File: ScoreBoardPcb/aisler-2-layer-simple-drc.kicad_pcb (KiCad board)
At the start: 2 copper layers, 95 x 75 mm, 16 parts, among them J1 Conn_02x20_Odd_Even, U1 CD4066BM96, U2 CD4066BM96, U3 CD4066BM96, U4 CD4066BM96, U5 ADM3101EARQZ-REEL

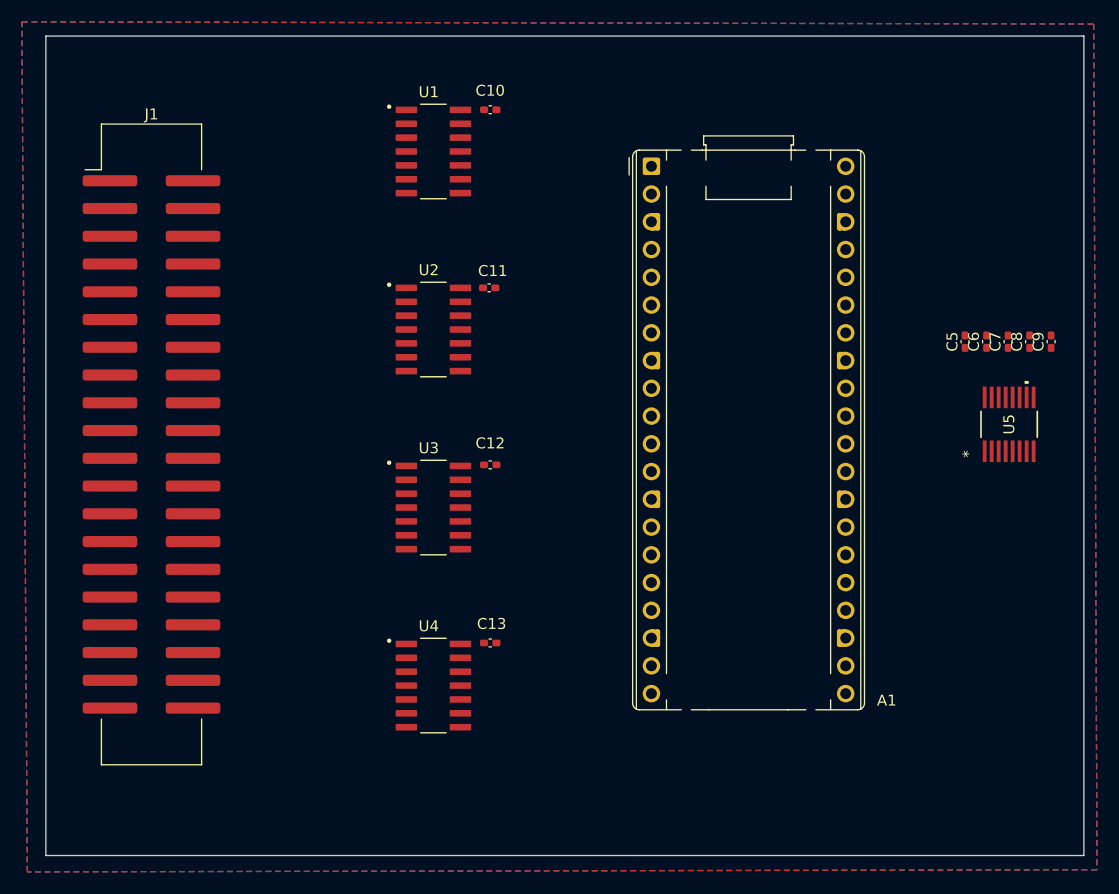
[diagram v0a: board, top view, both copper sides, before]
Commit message: Routed with mounting holes
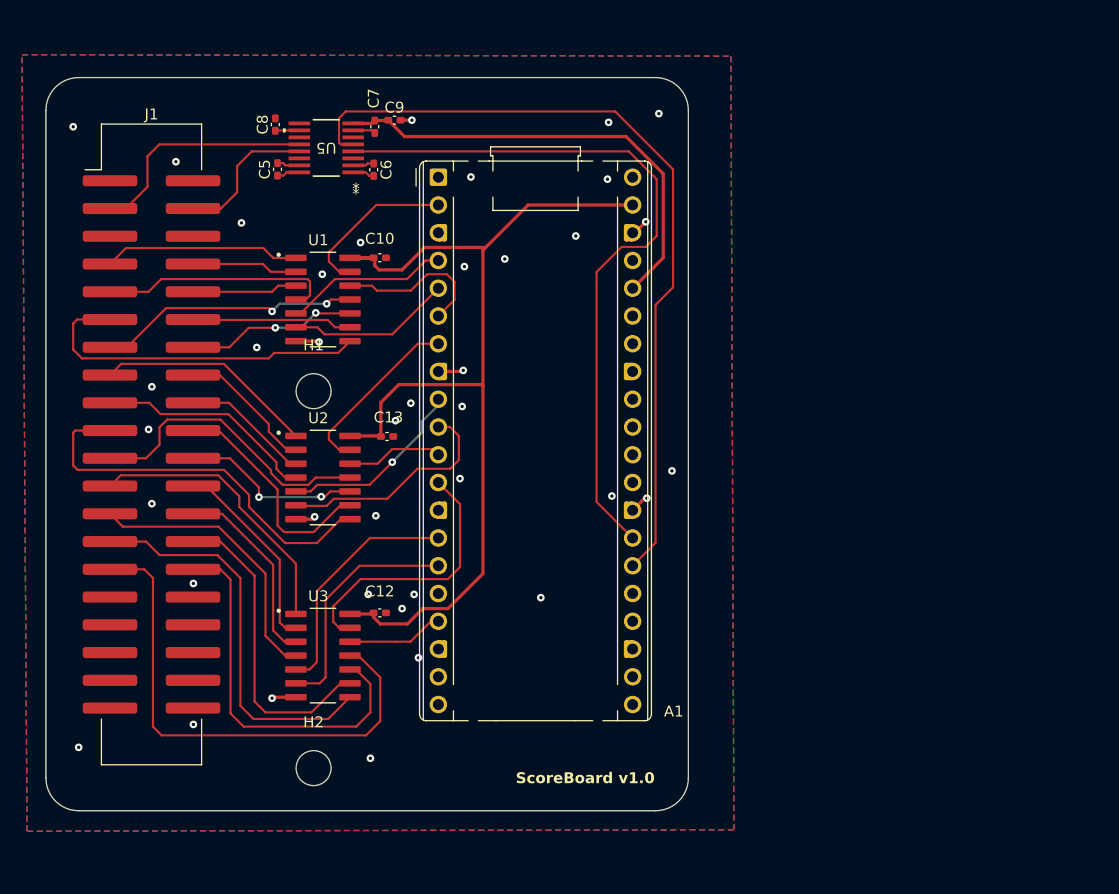
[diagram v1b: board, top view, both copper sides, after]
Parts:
- removed C11: 0.1uF, Capacitor_SMD:C_0402_1005Metric_Pad0.74x0.62mm_HandSolder
- removed U4: CD4066BM96, ScoreBoardPcb:SOIC127P600X175-14N
- added H1: MountingHole, MountingHole:MountingHole_3.2mm_M3, F.Cu at (124.5, 82.5)
- added H2: MountingHole, MountingHole:MountingHole_3.2mm_M3, F.Cu at (124.5, 117.0)
- moved C8 71.8 mm to (121.0, 58.1)
- moved U5 67.4 mm to (125.7, 60.2), turned to 180 degrees
- moved C5 64.9 mm to (121.2, 62.2)
- moved C9 63.4 mm to (131.9, 57.7), turned to 0 degrees
- moved C7 61.2 mm to (130.1, 58.3), turned to -90 degrees
- moved C6 58.3 mm to (130.0, 62.2), turned to -90 degrees
- moved C13 21.1 mm to (131.2, 86.6)
- moved A1 19.5 mm to (135.9, 62.9)
- moved C10 16.9 mm to (130.6, 70.3)
- moved U1 16.9 mm to (125.4, 74.1)
- moved U2 16.9 mm to (125.4, 90.4)
- moved U3 16.9 mm to (125.4, 106.7)
- moved C12 16.9 mm to (130.6, 102.8)
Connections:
- A1 pad 10: unconnected-(A1-GPIO7-Pad10) -> /MIN_INC
- A1 pad 11: unconnected-(A1-GPIO8-Pad11) -> /MIN_DEC
- A1 pad 12: unconnected-(A1-GPIO9-Pad12) -> /SEC_INC
- A1 pad 14: unconnected-(A1-GPIO10-Pad14) -> /SEC_DEC
- A1 pad 15: unconnected-(A1-GPIO11-Pad15) -> /CLEAR
- A1 pad 17: unconnected-(A1-GPIO13-Pad17) -> /AUX
- A1 pad 21: /TX_TTL -> unconnected-(A1-GPIO16-Pad21)
- A1 pad 22: /RX_TTL -> unconnected-(A1-GPIO17-Pad22)
- A1 pad 26: unconnected-(A1-GPIO20-Pad26) -> /TX_TTL
- A1 pad 27: unconnected-(A1-GPIO21-Pad27) -> /RX_TTL
- J1 pad 19: unconnected-(J1-Pin_19-Pad19) -> /MIN_INC_1
- J1 pad 20: unconnected-(J1-Pin_20-Pad20) -> /MIN_INC_2
- J1 pad 21: unconnected-(J1-Pin_21-Pad21) -> /MIN_DEC_1
- J1 pad 22: unconnected-(J1-Pin_22-Pad22) -> /MIN_DEC_2
- J1 pad 23: unconnected-(J1-Pin_23-Pad23) -> /SEC_INC_1
- J1 pad 24: unconnected-(J1-Pin_24-Pad24) -> /SEC_INC_2
- J1 pad 25: unconnected-(J1-Pin_25-Pad25) -> /SEC_DEC_1
- J1 pad 26: unconnected-(J1-Pin_26-Pad26) -> /SEC_DEC_2
- J1 pad 27: unconnected-(J1-Pin_27-Pad27) -> /CLEAR_1
- J1 pad 28: unconnected-(J1-Pin_28-Pad28) -> /CLEAR_2
- J1 pad 29: unconnected-(J1-Pin_29-Pad29) -> /AUX_1
- J1 pad 30: unconnected-(J1-Pin_30-Pad30) -> /AUX_2
- J1 pad 31: unconnected-(J1-Pin_31-Pad31) -> GND
- J1 pad 32: unconnected-(J1-Pin_32-Pad32) -> GND
- J1 pad 33: unconnected-(J1-Pin_33-Pad33) -> GND
- J1 pad 34: unconnected-(J1-Pin_34-Pad34) -> GND
- J1 pad 35: unconnected-(J1-Pin_35-Pad35) -> GND
- J1 pad 36: unconnected-(J1-Pin_36-Pad36) -> GND
- J1 pad 37: unconnected-(J1-Pin_37-Pad37) -> GND
- J1 pad 38: unconnected-(J1-Pin_38-Pad38) -> GND
- J1 pad 39: unconnected-(J1-Pin_39-Pad39) -> GND
- J1 pad 40: unconnected-(J1-Pin_40-Pad40) -> GND
- J1 pad 5: unconnected-(J1-Pin_5-Pad5) -> GND
- J1 pad 6: unconnected-(J1-Pin_6-Pad6) -> GND
- U2 pad 10: unconnected-(U2-SIG_D_OUT/IN-Pad10) -> /MIN_DEC_2
- U2 pad 11: unconnected-(U2-SIG_D_IN/OUT-Pad11) -> /MIN_DEC_1
- U2 pad 12: unconnected-(U2-CONTROL_D-Pad12) -> /MIN_DEC
- U2 pad 6: unconnected-(U2-CONTROL_C-Pad6) -> /MIN_INC
- U2 pad 8: unconnected-(U2-SIG_C_IN/OUT-Pad8) -> /MIN_INC_1
- U2 pad 9: unconnected-(U2-SIG_C_OUT/IN-Pad9) -> /MIN_INC_2
- U3 pad 1: unconnected-(U3-SIG_A_IN/OUT-Pad1) -> /SEC_INC_1
- U3 pad 10: unconnected-(U3-SIG_D_OUT/IN-Pad10) -> /AUX_2
- U3 pad 11: unconnected-(U3-SIG_D_IN/OUT-Pad11) -> /AUX_1
- U3 pad 12: unconnected-(U3-CONTROL_D-Pad12) -> /AUX
- U3 pad 13: unconnected-(U3-CONTROL_A-Pad13) -> /SEC_INC
- U3 pad 2: unconnected-(U3-SIG_A_OUT/IN-Pad2) -> /SEC_INC_2
- U3 pad 3: unconnected-(U3-SIG_B_OUT/IN-Pad3) -> /SEC_DEC_2
- U3 pad 4: unconnected-(U3-SIG_B_IN/OUT-Pad4) -> /SEC_DEC_1
- U3 pad 5: unconnected-(U3-CONTROL_B-Pad5) -> /SEC_DEC
- U3 pad 6: unconnected-(U3-CONTROL_C-Pad6) -> /CLEAR
- U3 pad 8: unconnected-(U3-SIG_C_IN/OUT-Pad8) -> /CLEAR_1
- U3 pad 9: unconnected-(U3-SIG_C_OUT/IN-Pad9) -> /CLEAR_2
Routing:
- net +5V: track 0.00 -> 91.7 mm
- net /TX_TTL: track 0.00 -> 74.4 mm
- net /RX_TTL: track 0.00 -> 66.6 mm
- net /AUX_1: track 0.00 -> 47.1 mm
- net +3.3V: track 0.00 -> 42.1 mm
- net /CLEAR_1: track 0.00 -> 36.4 mm
- net /MIN_INC_1: track 0.00 -> 35.4 mm
- net /AUX_2: track 0.00 -> 34.9 mm
- net /HOME_DEC_1: track 0.00 -> 32.2 mm
- net /CLEAR_2: track 0.00 -> 27.8 mm
- net /MIN_DEC_1: track 0.00 -> 27.3 mm
- net /SEC_INC_1: track 0.00 -> 26.0 mm
- net /SEC_DEC_1: track 0.00 -> 25.7 mm
- net /SEC_INC: track 0.00 -> 24.8 mm
- net /AWAY_INC_1: track 0.00 -> 22.8 mm, vias 0 -> 2
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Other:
- board size 95 x 75 mm -> 58.8 x 67.1 mm
- board text added: "ScoreBoard v1.0"

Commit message: Update to use CD74HCT4066M96
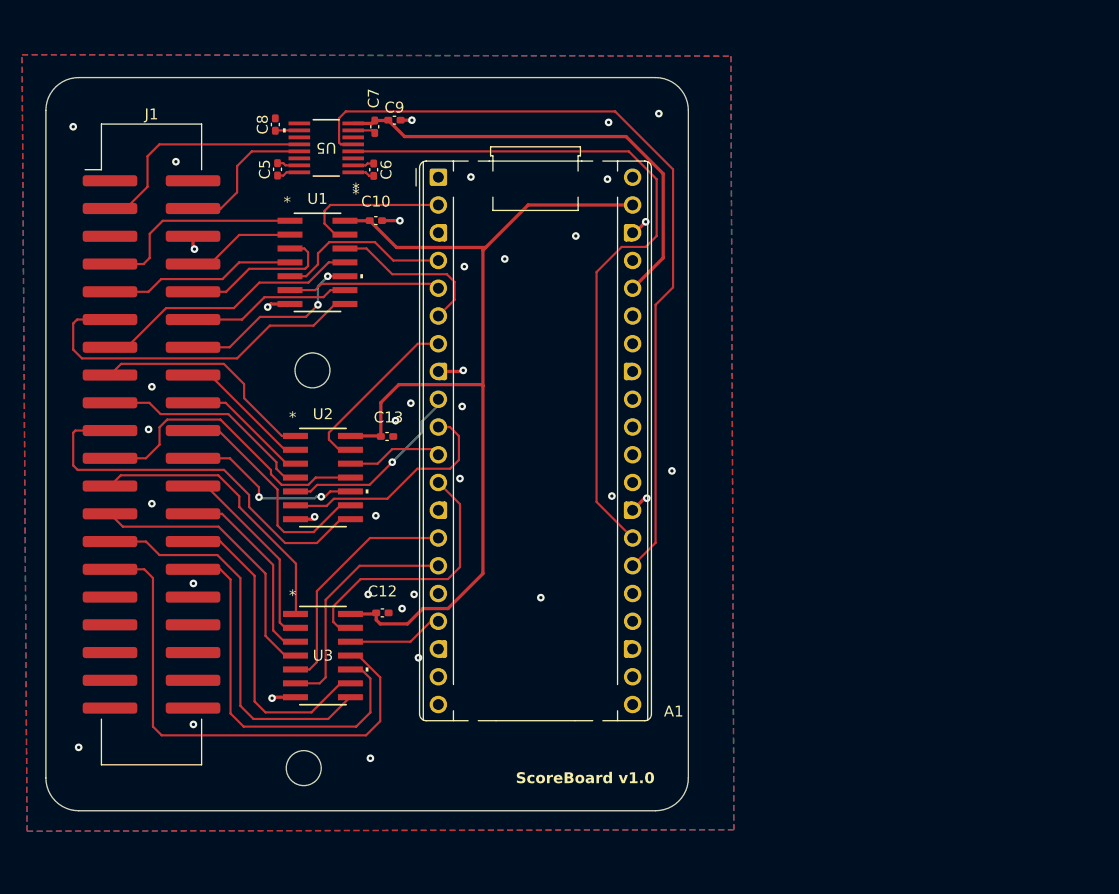
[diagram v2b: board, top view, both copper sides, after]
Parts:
- U1, U2, U3: value CD4066BM96 -> CD74HCT4066M96; footprint ScoreBoardPcb:SOIC127P600X175-14N -> ScoreBoardPcb:D14-M
- moved U1 3.44 mm to (124.9, 70.7)
- moved C10 3.42 mm to (130.2, 66.9)
- moved H1 1.90 mm to (124.4, 80.6)
- moved H2 0.90 mm to (123.6, 117.0)
- moved C12 0.24 mm to (130.8, 102.8)
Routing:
- net /HOME_INC_2: track 9.65 -> 14.6 mm
- net /HOME_INC_1: track 21.6 -> 17.6 mm
- net GND: track 12.9 -> 15.6 mm, vias 39 -> 37
- net /AWAY_DEC_2: track 11.8 -> 9.68 mm
- net +5V: track 91.7 -> 89.6 mm
- net /AWAY_INC_2: track 15.7 -> 17.6 mm
- net /START: track 15.0 -> 13.2 mm
- net /HOME_DEC: track 15.1 -> 13.4 mm
- net /HOME_INC: track 14.6 -> 16.2 mm
- net /START_1: track 18.0 -> 19.4 mm
- net /START_2: track 9.71 -> 8.39 mm
- net /SEC_DEC_2: track 17.4 -> 16.4 mm
- net /AWAY_DEC: track 16.3 -> 15.4 mm
- net /SEC_INC: track 24.8 -> 23.8 mm
- net /SEC_INC_2: track 16.9 -> 16.0 mm
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
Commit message: Rev 1.0 submitted for manf
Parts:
- A1: footprint Module:RaspberryPi_Pico_Common_THT -> ScoreBoardPcb:RaspberryPi_Pico_Common_THT
- moved H1 26.5 mm to (120.5, 54.4)
- moved C8 6.44 mm to (119.9, 64.4), turned to 180 degrees
- moved U5 5.79 mm to (124.9, 66.0)
- moved C5 5.78 mm to (120.6, 67.9)
- moved C6 5.77 mm to (129.5, 68.0)
- moved C7 5.77 mm to (129.6, 64.0)
- moved C9 5.77 mm to (131.4, 63.4)
- moved C10 5.75 mm to (130.4, 72.6)
- moved U1 5.75 mm to (124.9, 76.5)
- moved U3 4.52 mm to (124.8, 102.2)
- moved C12 4.42 mm to (130.3, 98.4)
- moved H2 3.16 mm to (120.5, 116.4)
- moved C13 1.47 mm to (130.3, 85.5)
- moved U2 1.18 mm to (124.9, 89.3)
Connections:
- A1 pad 39: +5V -> unconnected-(A1-VSYS-Pad39)
- J1 pad 2: GND -> +5V
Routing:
- net /AUX_2: track 34.2 -> 12.6 mm, vias 0 -> 2
- net /TX_TTL: track 74.4 -> 61.7 mm
- net /AUX_1: track 46.4 -> 34.0 mm
- net /CLEAR_2: track 27.8 -> 15.6 mm
- net +5V: track 89.6 -> 100.4 mm
- net /CLEAR_1: track 36.4 -> 26.4 mm
- net /RX_TTL: track 66.6 -> 56.9 mm
- net /HOME_DEC_2: track 15.0 -> 24.0 mm
- net /SEC_INC: track 23.8 -> 15.5 mm
- net /MIN_INC_1: track 35.4 -> 27.6 mm
- net /MIN_DEC: track 8.86 -> 15.8 mm
- net /SEC_DEC_2: track 16.4 -> 9.55 mm
- net /SEC_INC_1: track 26.0 -> 19.2 mm
- net /AWAY_DEC_2: track 9.68 -> 16.1 mm
- net /AWAY_INC: track 15.0 -> 8.62 mm
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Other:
- board size 58.8 x 67.1 mm -> 59 x 71 mm
